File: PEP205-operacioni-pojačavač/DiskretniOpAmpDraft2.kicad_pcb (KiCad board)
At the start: 2 copper layers, 90 x 45 mm, 41 parts, among them J1 J111, J2 Ulazi, J3 Izlaz, J4 +9V, J5 GND, J6 -9V, J7 KlasaABIzlaz, J8 J111, Q10 NPN, Q11 NPN, Q12 NPN, Q13 NPN, Q14 PNP, Q3 PNP, Q4 PNP, Q5 NPN, Q6 PNP, Q7 PNP, Q8 PNP, Q9 NPN

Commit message: fixed 205 shield issues
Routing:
- net GND: vias 4 -> 174
- net (no net): vias 170 -> 0

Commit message: removed edge copper graphic, poured ground on top, removed excess via.
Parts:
- removed REF**: ele_petnica_logo, PEP_library:ele_petnica_logo
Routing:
- net GND: vias 174 -> 173
- added copper zone on F.Cu, net GND

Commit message: zbrzano dodati konektori na drugačiji način
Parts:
- removed J2: Ulazi, Connector_PinSocket_2.54mm:PinSocket_1x03_P2.54mm_Vertical
- added J10: Izlaz, Connector_PinSocket_2.54mm:PinSocket_1x02_P2.54mm_Vertical, F.Cu at (174.8, 110.0)
- added J11: Ulaz, Connector_PinSocket_2.54mm:PinSocket_1x02_P2.54mm_Vertical, F.Cu at (110.7, 133.1)
- added J12: Ulaz, Connector_PinSocket_2.54mm:PinSocket_1x02_P2.54mm_Vertical, F.Cu at (110.7, 139.7)
- added J9: Ulaz, Connector_PinSocket_2.54mm:PinSocket_1x02_P2.54mm_Vertical, F.Cu at (110.9, 146.7)
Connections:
- J3 pad 2: GND -> /izlaz
- J7 pad 2: GND -> /klasaABizlaz
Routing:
- net GND: track 16.2 -> 6.15 mm, vias 173 -> 170
- net /izlaz: track 64.0 -> 69.1 mm
- net /klasaABizlaz: track 19.5 -> 17.7 mm

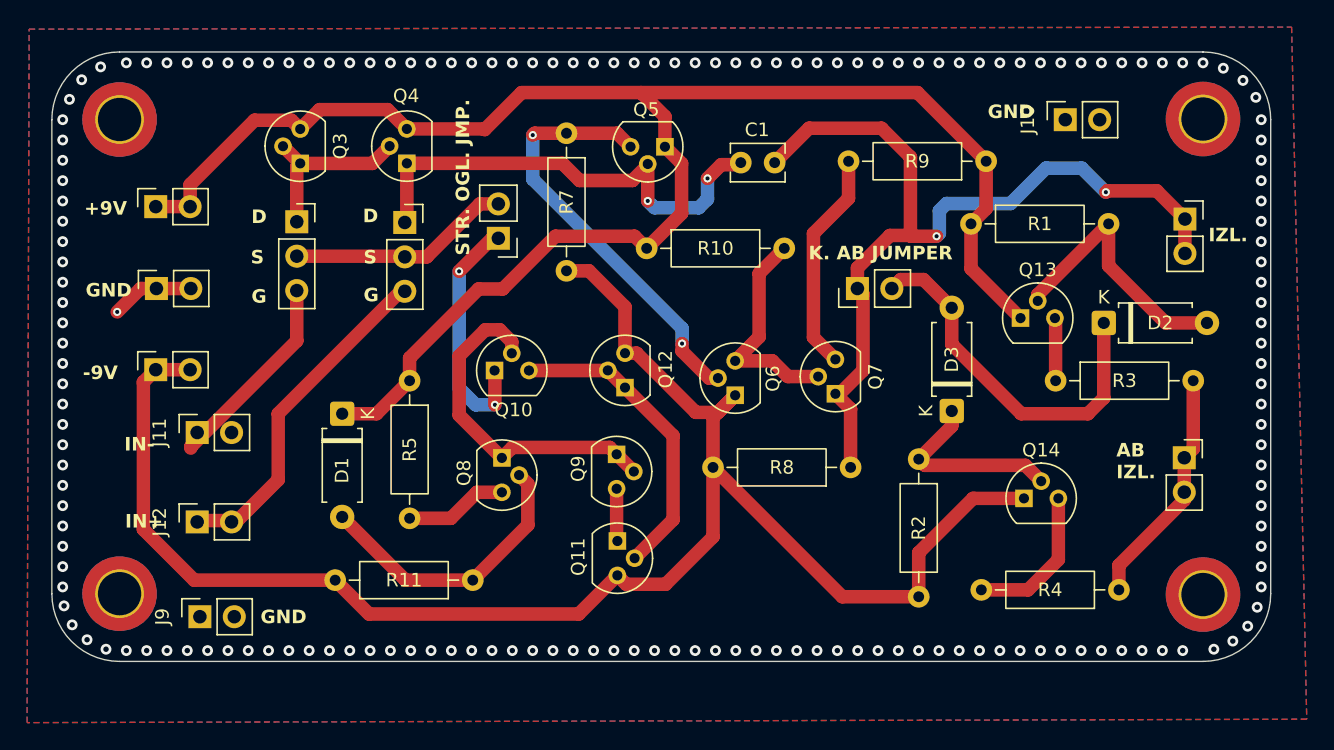
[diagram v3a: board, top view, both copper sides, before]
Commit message: Dodat još jedan tranzistor da bi se formiralo Vilsonovo ogledalo sa 3 tranzistora kod diferencijalnog para
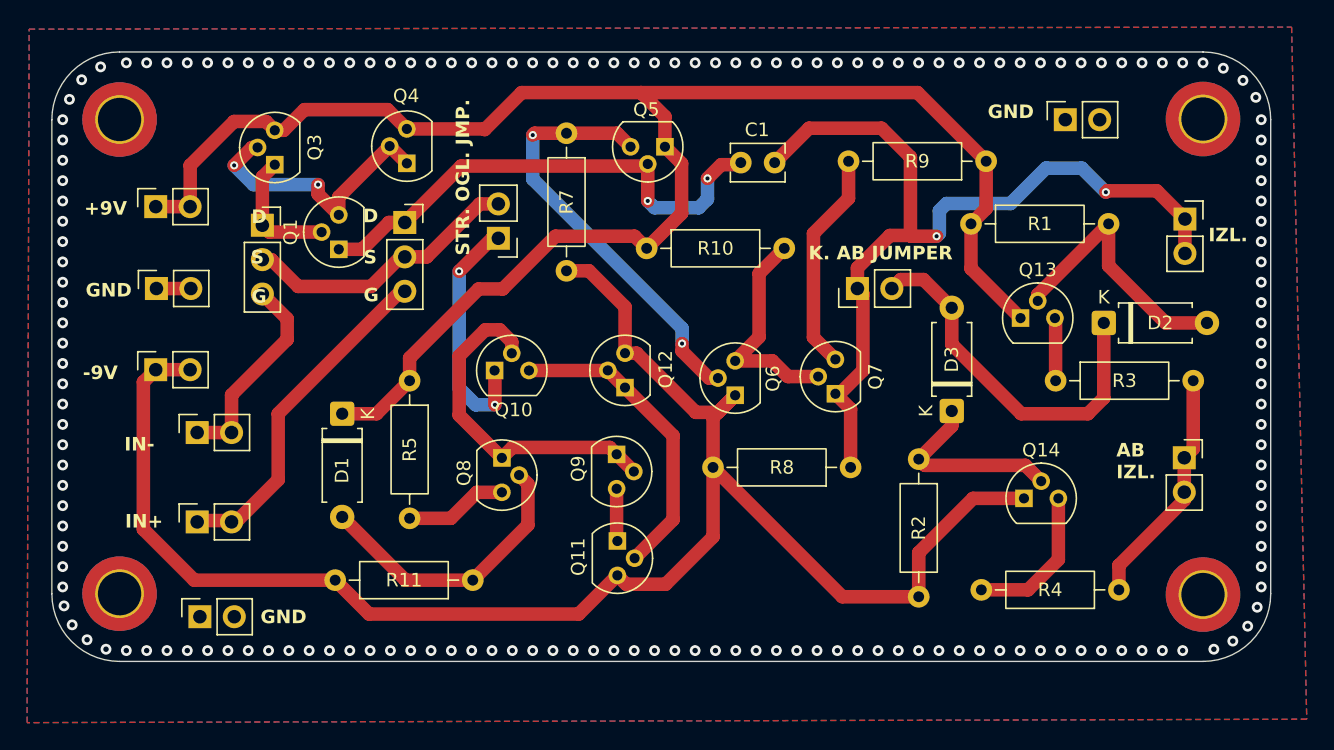
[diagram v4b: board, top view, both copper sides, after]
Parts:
- added Q1: PNP, Package_TO_SOT_THT:TO-92, F.Cu at (121.2, 119.6)
- moved J1 2.55 mm to (115.5, 117.8)
- moved Q3 1.88 mm to (116.5, 113.3)
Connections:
- Q3 pad 2: Net-(J1-Pin_1) -> Net-(Q1-E)
- Q4 pad 1: Net-(J8-Pin_1) -> Net-(Q1-E)
- Q4 pad 2: Net-(J1-Pin_1) -> Net-(Q1-E)
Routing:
- net Net-(Q1-E): track 0.00 -> 20.4 mm, vias 0 -> 2
- net /StrOgl: track 16.5 -> 20.8 mm
- net Net-(J1-Pin_1): track 13.3 -> 9.43 mm
- net GND: track 6.15 -> 2.54 mm, vias 170 -> 169
- net Net-(J8-Pin_1): track 35.4 -> 37.6 mm
- net +9V: track 126.3 -> 127.1 mm

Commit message: changed some footprints, some BL traces
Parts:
- Q10, Q3, Q5, Q9: footprint Package_TO_SOT_THT:TO-92 -> Package_TO_SOT_THT:TO-92L_Inline
- moved Q5 3.62 mm to (142.0, 113.5), turned to 0 degrees
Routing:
- net Net-(Q10-B): track 25.5 -> 16.7 mm
- net Net-(JP1-A): track 18.2 -> 9.93 mm, vias 2 -> 0
- net /izlaz: track 69.1 -> 64.1 mm, vias 2 -> 0
- net Net-(Q1-E): track 20.4 -> 16.1 mm, vias 2 -> 0
- net Net-(Q5-E): track 31.8 -> 29.7 mm, vias 2 -> 0
- net Net-(Q10-E): track 22.9 -> 21.5 mm
- net +9V: track 127.1 -> 126.0 mm, vias 0 -> 1
- net Net-(J8-Pin_1): track 37.6 -> 37.7 mm, vias 2 -> 0

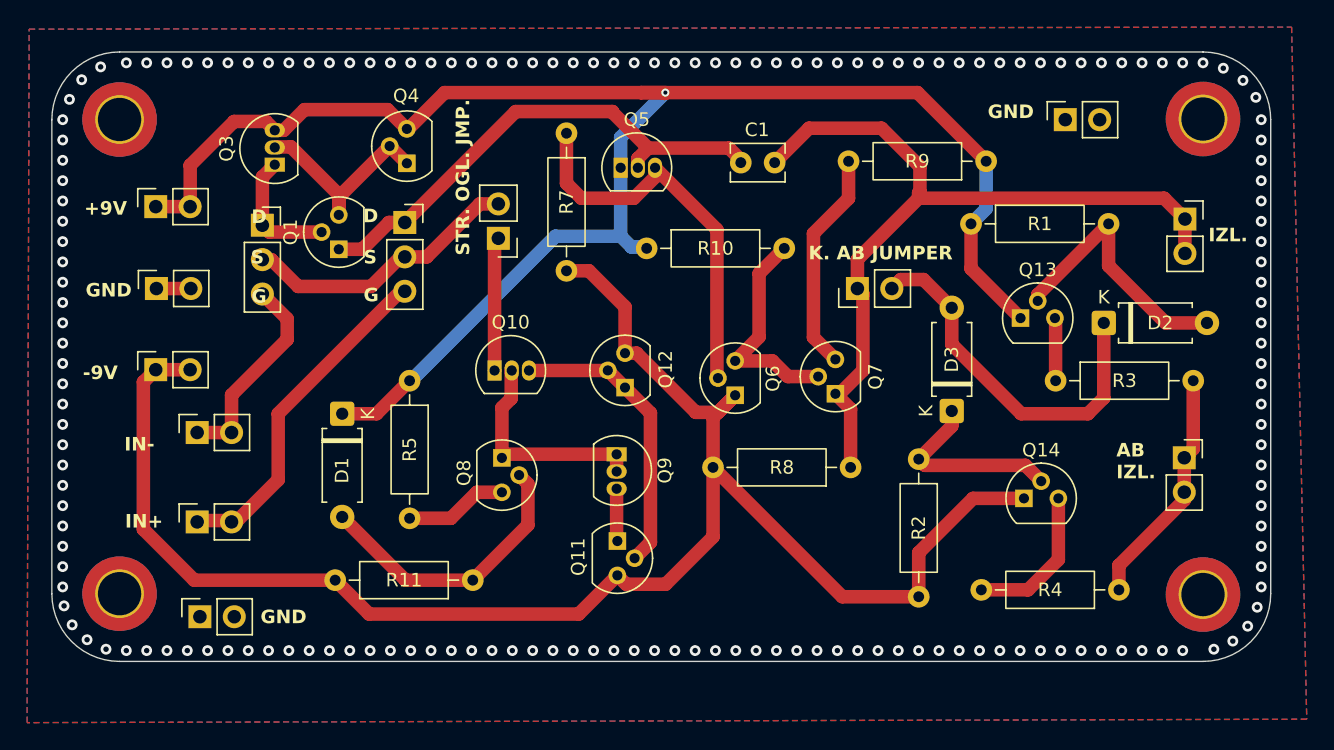
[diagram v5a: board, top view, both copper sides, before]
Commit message: Napravljene sitne estetske izmene(malo pomeranje komponenata).
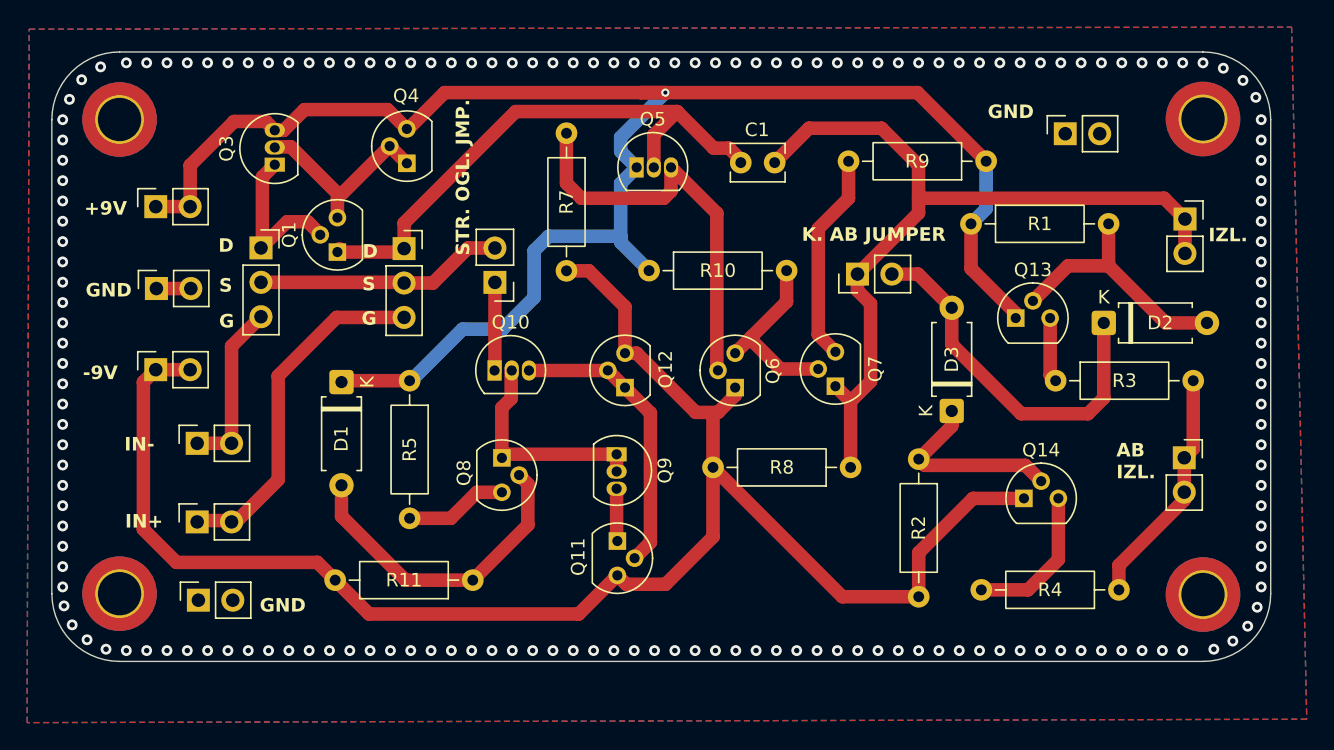
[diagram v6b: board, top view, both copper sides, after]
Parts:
- moved JP1 3.27 mm to (132.7, 122.0)
- moved D1 2.34 mm to (121.4, 129.4)
- moved J8 1.93 mm to (126.0, 119.5)
- moved J1 1.68 mm to (115.4, 119.5)
- moved R10 1.65 mm to (144.1, 121.1)
- moved J9 1.23 mm to (110.8, 145.5)
- moved Q5 1.18 mm to (143.2, 113.5)
- moved JP2 1.07 mm to (159.5, 121.4)
- moved J10 1.04 mm to (174.8, 111.0)
- moved J11 0.80 mm to (110.7, 133.9)
- moved Q6 0.57 mm to (150.5, 129.8)
- moved Q7 0.56 mm to (157.9, 129.7)
- moved Q13 0.36 mm to (171.2, 124.7)
- moved Q1 0.23 mm to (121.1, 119.8)
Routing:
- net Net-(J8-Pin_1): track 37.7 -> 42.1 mm
- net Net-(JP1-A): track 9.93 -> 6.55 mm
- net +9V: track 126.0 -> 129.1 mm
- net Net-(Q6-E): track 16.6 -> 13.6 mm
- net Net-(J1-Pin_1): track 9.43 -> 12.2 mm
- net /StrOgl: track 20.8 -> 18.4 mm
- net /invert: track 15.2 -> 12.8 mm
- net -9V: track 124.5 -> 122.8 mm
- net Net-(D1-A): track 21.3 -> 22.7 mm
- net Net-(Q1-E): track 16.1 -> 14.8 mm
- net Net-(D2-A): track 20.0 -> 18.8 mm
- net Net-(Q7-E): track 16.6 -> 15.5 mm
- net /izlaz: track 64.1 -> 64.9 mm
- net /neinvert: track 24.9 -> 25.7 mm
- net Net-(Q5-E): track 29.7 -> 30.4 mm
